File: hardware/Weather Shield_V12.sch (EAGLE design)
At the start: 52 parts, among them J1 GP-735, Q1 200mA/50V, Q2 200mA/50V, U1 ARDUINO_R3_SHIELD, U3 ALS-PT19, U4 MPL3115A2LGA8, U5 SI7021, U6 3.3V/150mA

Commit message: Slight modifications before final review
Moved logos to avoid cover up by GPS. Moved GPS backup batter
connection. Change jumper on D12 to NO instead of NC.
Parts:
- JP1: value JUMPER-PAD-2-NC_BY_TRACENO_SILK -> JUMPER-PAD-2-NO; device SparkFun-Passives:JUMPER-PAD-2-NC_BY_TRACENO_SILK -> SparkFun-Passives:JUMPER-PAD-2-NO
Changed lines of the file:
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@@
 <grid distance="0.1" unitdist="inch" unit="inch" style="lines" multiple="1" display="no" altdistance="0.01" altunitdist="inch" altunit="inch"/>
 <layers>
-<layer number="1" name="Top" color="4" fill="1" visible="no" active="no"/>
-<layer number="2" name="Route2" color="1" fill="3" visible="no" active="no"/>
-<layer number="3" name="Route3" color="4" fill="3" visible="no" active="no"/>
-<layer number="4" name="Route4" color="1" fill="4" visible="no" active="no"/>
-<layer number="5" name="Route5" color="4" fill="4" visible="no" active="no"/>
-<layer number="6" name="Route6" color="1" fill="8" visible="no" active="no"/>
-<layer number="7" name="Route7" color="4" fill="8" visible="no" active="no"/>
-<layer number="8" name="Route8" color="1" fill="2" visible="no" active="no"/>
-<layer number="9" name="Route9" color="4" fill="2" visible="no" active="no"/>
-<layer number="10" name="Route10" color="1" fill="7" visible="no" active="no"/>
-<layer number="11" name="Route11" color="4" fill="7" visible="no" active="no"/>
-<layer number="12" name="Route12" color="1" fill="5" visible="no" active="no"/>
-<layer number="13" name="Route13" color="4" fill="5" visible="no" active="no"/>
-<layer number="14" name="Route14" color="1" fill="6" visible="no" active="no"/>
-<layer number="15" name="Route15" color="4" fill="6" visible="no" active="no"/>
-<layer number="16" name="Bottom" color="1" fill="1" visible="no" active="no"/>
-<layer number="17" name="Pads" color="2" fill="1" visible="no" active="no"/>
-<layer number="18" name="Vias" color="2" fill="1" visible="no" active="no"/>
-<layer number="19" name="Unrouted" color="6" fill="1" visible="no" active="no"/>
-<layer number="20" name="Dimension" color="15" fill="1" visible="no" active="no"/>
-<layer number="21" name="tPlace" color="16" fill="1" visible="no" active="no"/>
-<layer number="22" name="bPlace" color="14" fill="1" visible="no" active="no"/>
-<layer number="23" name="tOrigins" color="15" fill="1" visible="no" active="no"/>
-<layer number="24" name="bOrigins" color="15" fill="1" visible="no" active="no"/>
-<layer number="25" name="tNames" color="7" fill="1" visible="no" active="no"/>
-<layer number="26" name="bNames" color="7" fill="1" visible="no" active="no"/>
-<layer number="27" name="tValues" color="7" fill="1" visible="no" active="no"/>
-<layer number="28" name="bValues" color="7" fill="1" visible="no" active="no"/>
+<layer number="1" name="Top" color="4" fill="1" visible="yes" active="no"/>
+<layer number="2" name="Route2" color="1" fill="3" visible="yes" active="no"/>
+<layer number="3" name="Route3" color="4" fill="3" visible="yes" active="no"/>
+<layer number="4" name="Route4" color="1" fill="4" visible="yes" active="no"/>
+<layer number="5" name="Route5" color="4" fill="4" visible="yes" active="no"/>
+<layer number="6" name="Route6" color="1" fill="8" visible="yes" active="no"/>
+<layer number="7" name="Route7" color="4" fill="8" visible="yes" active="no"/>
+<layer number="8" name="Route8" color="1" fill="2" visible="yes" active="no"/>
+<layer number="9" name="Route9" color="4" fill="2" visible="yes" active="no"/>
+<layer number="10" name="Route10" color="1" fill="7" visible="yes" active="no"/>
+<layer number="11" name="Route11" color="4" fill="7" visible="yes" active="no"/>
+<layer number="12" name="Route12" color="1" fill="5" visible="yes" active="no"/>
+<layer number="13" name="Route13" color="4" fill="5" visible="yes" active="no"/>
+<layer number="14" name="Route14" color="1" fill="6" visible="yes" active="no"/>
+<layer number="15" name="Route15" color="4" fill="6" visible="yes" active="no"/>
+<layer number="16" name="Bottom" color="1" fill="1" visible="yes" active="no"/>
+<layer number="17" name="Pads" color="2" fill="1" visible="yes" active="no"/>
+<layer number="18" name="Vias" color="2" fill="1" visible="yes" active="no"/>
+<layer number="19" name="Unrouted" color="6" fill="1" visible="yes" active="no"/>
+<layer number="20" name="Dimension" color="15" fill="1" visible="yes" active="no"/>
+<layer number="21" name="tPlace" color="16" fill="1" visible="yes" active="no"/>
+<layer number="22" name="bPlace" color="14" fill="1" visible="yes" active="no"/>
+<layer number="23" name="tOrigins" color="15" fill="1" visible="yes" active="no"/>
+<layer number="24" name="bOrigins" color="15" fill="1" visible="yes" active="no"/>
+<layer number="25" name="tNames" color="7" fill="1" visible="yes" active="no"/>
+<layer number="26" name="bNames" color="7" fill="1" visible="yes" active="no"/>
+<layer number="27" name="tValues" color="7" fill="1" visible="yes" active="no"/>
+<layer number="28" name="bValues" color="7" fill="1" visible="yes" active="no"/>
 <layer number="29" name="tStop" color="7" fill="3" visible="no" active="no"/>
 <layer number="30" name="bStop" color="7" fill="6" visible="no" active="no"/>
@@
 <layer number="35" name="tGlue" color="7" fill="4" visible="no" active="no"/>
 <layer number="36" name="bGlue" color="7" fill="5" visible="no" active="no"/>
-<layer number="37" name="tTest" color="7" fill="1" visible="no" active="no"/>
-<layer number="38" name="bTest" color="7" fill="1" visible="no" active="no"/>
+<layer number="37" name="tTest" color="7" fill="1" visible="yes" active="no"/>
+<layer number="38" name="bTest" color="7" fill="1" visible="yes" active="no"/>
 <layer number="39" name="tKeepout" color="4" fill="11" visible="no" active="no"/>
 <layer number="40" name="bKeepout" color="1" fill="11" visible="no" active="no"/>
@@
 <layer number="44" name="Drills" color="7" fill="1" visible="no" active="no"/>
 <layer number="45" name="Holes" color="7" fill="1" visible="no" active="no"/>
-<layer number="46" name="Milling" color="3" fill="1" visible="no" active="no"/>
-<layer number="47" name="Measures" color="7" fill="1" visible="no" active="no"/>
-<layer number="48" name="Document" color="7" fill="1" visible="no" active="no"/>
-<layer number="49" name="Reference" color="7" fill="1" visible="no" active="no"/>
-<layer number="50" name="dxf" color="7" fill="1" visible="no" active="no"/>
-<layer number="51" name="tDocu" color="6" fill="1" visible="no" active="no"/>
-<layer number="52" name="bDocu" color="7" fill="1" visible="no" active="no"/>
-<layer number="53" name="tGND_GNDA" color="7" fill="9" visible="no" active="no"/>
-<layer number="54" name="bGND_GNDA" color="1" fill="9" visible="no" active="no"/>
-<layer number="56" name="wert" color="7" fill="1" visible="no" active="no"/>
-<layer number="57" name="tCAD" color="7" fill="1" visible="no" active="no"/>
-<layer number="59" name="tCarbon" color="7" fill="1" visible="no" active="no"/>
-<layer number="60" name="bCarbon" color="7" fill="1" visible="no" active="no"/>
+<layer number="46" name="Milling" color="3" fill="1" visible="yes" active="no"/>
+<layer number="47" name="Measures" color="7" fill="1" visible="yes" active="no"/>
+<layer number="48" name="Document" color="7" fill="1" visible="yes" active="no"/>
+<layer number="49" name="Reference" color="7" fill="1" visible="yes" active="no"/>
+<layer number="50" name="dxf" color="7" fill="1" visible="yes" active="no"/>
+<layer number="51" name="tDocu" color="6" fill="1" visible="yes" active="no"/>
+<layer number="52" name="bDocu" color="7" fill="1" visible="yes" active="no"/>
+<layer number="53" name="tGND_GNDA" color="7" fill="9" visible="yes" active="no"/>
+<layer number="54" name="bGND_GNDA" color="1" fill="9" visible="yes" active="no"/>
+<layer number="56" name="wert" color="7" fill="1" visible="yes" active="no"/>
+<layer number="57" name="tCAD" color="7" fill="1" visible="yes" active="no"/>
+<layer number="59" name="tCarbon" color="7" fill="1" visible="yes" active="no"/>
+<layer number="60" name="bCarbon" color="7" fill="1" visible="yes" active="no"/>
 <layer number="90" name="Modules" color="5" fill="1" visible="yes" active="yes"/>
 <layer number="91" name="Nets" color="2" fill="1" visible="yes" active="yes"/>
@@
 <part name="SUPPLY8" library="SparkFun-Aesthetics" deviceset="VIN" device=""/>
 <part name="SUPPLY9" library="SparkFun-Aesthetics" deviceset="VIN" device=""/>
-<part name="JP1" library="SparkFun-Passives" deviceset="JUMPER-PAD-2-NC_BY_TRACE" device="NO_SILK" value=""/>
+<part name="JP1" library="SparkFun-Passives" deviceset="JUMPER-PAD-2-NO" device="" value="JUMPER-PAD-2-NO"/>
 <part name="U6" library="SparkFun-PowerIC" deviceset="V_REG_MIC5205" device="3.3V" value="3.3V/150mA"/>
 </parts>

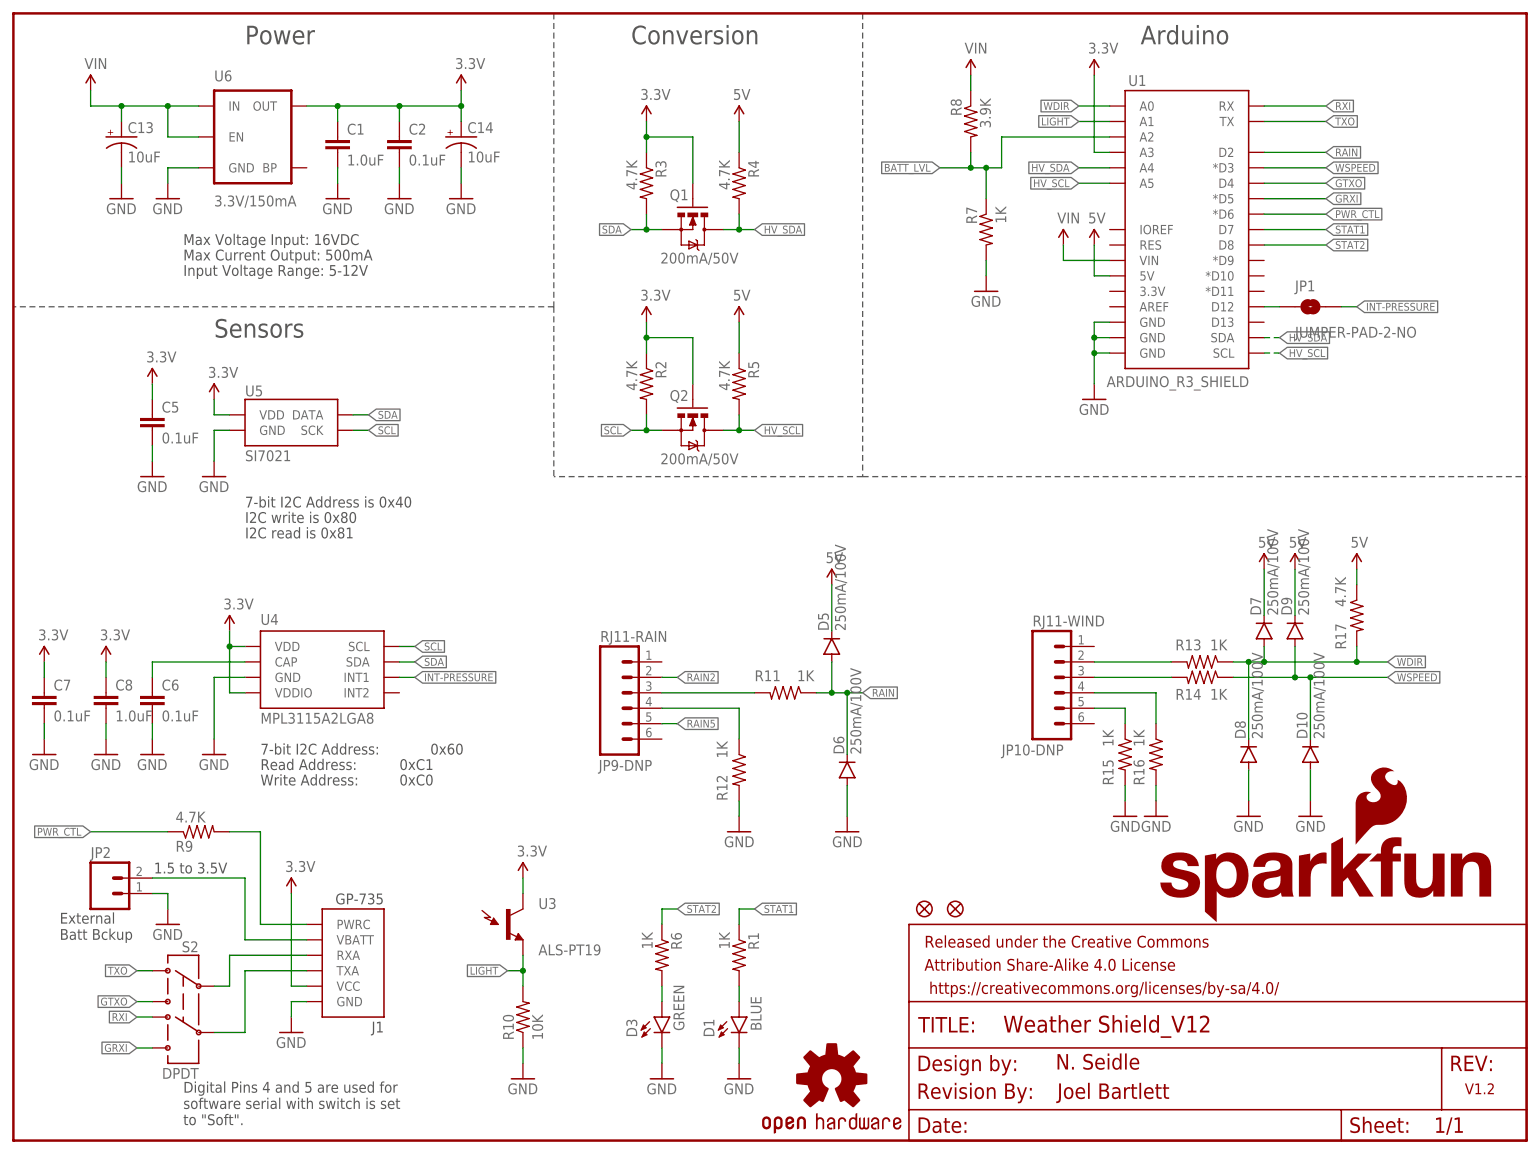
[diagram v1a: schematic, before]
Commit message: Minor Changes after group review for Reds
Fixed text under VREG to have correct info, fixed Eagle error on J1
(GPS Conn), fixed overlapping values, minor silk changes, moved via,
updated HW/SW serial switch text to modern standard .
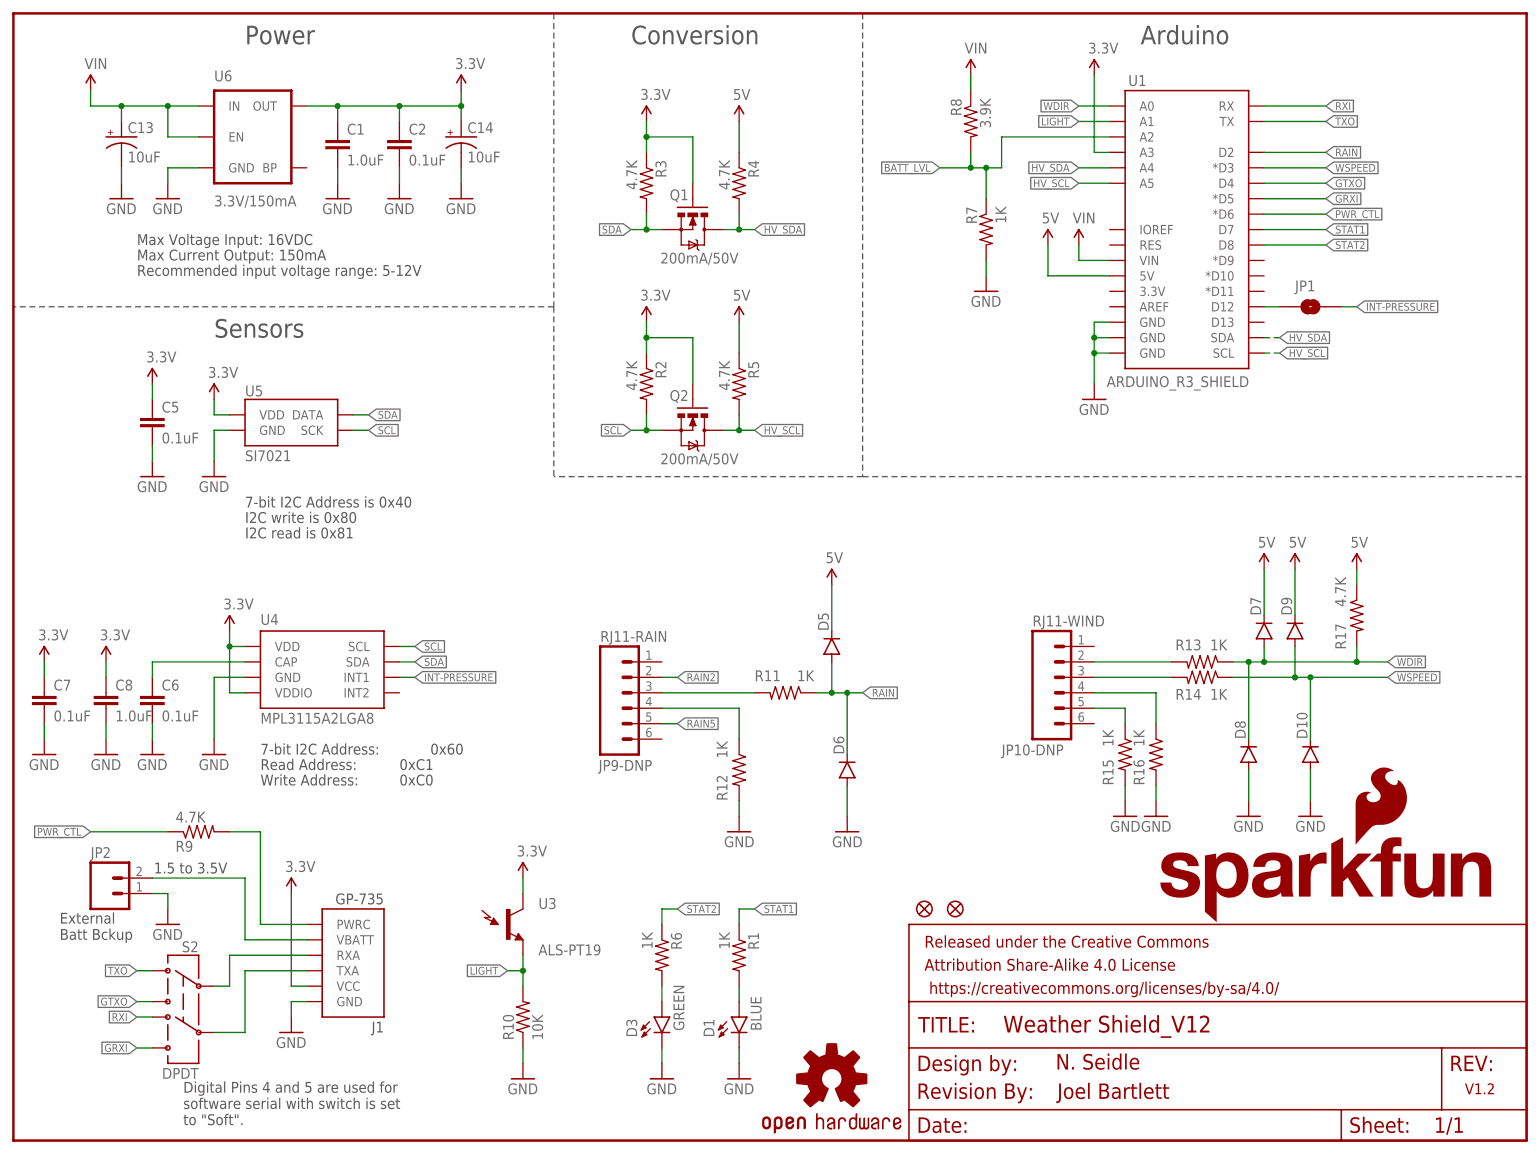
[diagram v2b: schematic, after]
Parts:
- D10, D5, D6, D7, D8, D9: value 250mA/100V -> (none)
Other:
- note added: "Max Current Output: 150mA"
- note added: "Recommended input voltage range: 5-12V"
- note removed: "Input Voltage Range: 5-12V"
- note removed: "Max Current Output: 500mA"

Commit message: Final issue fixes before going out for reds.
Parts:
- D10, D5, D6, D7, D8, D9: value (none) -> 250mA/100V
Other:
- note added: "Normally Open jumper for Interrupt 1 on MPL311"
- moved on the sheet: D7, D8, JP10-DNP, R13, R14, R15, R16
